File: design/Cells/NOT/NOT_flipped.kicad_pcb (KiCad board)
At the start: 2 copper layers, 2 parts, among them P1 Q_PJFET_GSD

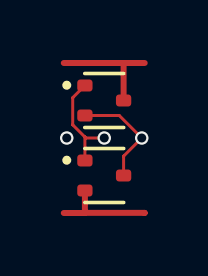
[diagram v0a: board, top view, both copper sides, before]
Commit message: All gates layout on a strict 2.5mm grid. Flipped versions of all three layouts
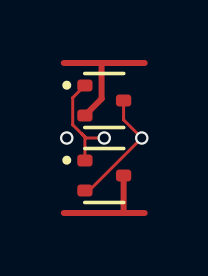
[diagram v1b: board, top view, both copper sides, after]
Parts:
- moved N1 2.50 mm to (1.25, 1.25)
- moved P1 2.50 mm to (1.25, 3.75)
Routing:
- net GND: track 3.45 -> 4.68 mm
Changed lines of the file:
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@@
 	(footprint "Package_TO_SOT_SMD:SOT-523"
 		(layer "F.Cu")
-		(at 1.25 1.25)
+		(at 1.25 3.75)
 		(descr "SOT523, https://www.diodes.com/assets/Package-Files/SOT523.pdf")
 		(tags "SOT-523")
@@
 	(footprint "Package_TO_SOT_SMD:SOT-523"
 		(layer "F.Cu")
-		(at 1.25 3.75)
+		(at 1.25 1.25)
 		(descr "SOT523, https://www.diodes.com/assets/Package-Files/SOT523.pdf")
 		(tags "SOT-523")
@@
 	)
 	(segment
-		(start 1.895 3.105)
-		(end 1.895 3.75)
+		(start 0.75 4.25)
+		(end 0.605 4.25)
 		(width 0.1)
 		(layer "F.Cu")
@@
 	)
 	(segment
-		(start 1.75 1.75)
+		(start 1.895 1.25)
+		(end 1.895 1.895)
+		(width 0.1)
+		(layer "F.Cu")
+		(net 1)
+	)
+	(segment
+		(start 1.895 1.895)
 		(end 2.5 2.5)
 		(width 0.1)
@@
 	)
 	(segment
-		(start 0.605 1.75)
-		(end 1.75 1.75)
-		(width 0.1)
-		(layer "F.Cu")
-		(net 1)
-	)
-	(segment
 		(start 2.5 2.5)
-		(end 1.895 3.105)
+		(end 0.75 4.25)
 		(width 0.1)
 		(layer "F.Cu")
@@
 	)
 	(segment
-		(start 0.605 4.995)
-		(end 2.595 4.995)
+		(start -0.1 0)
+		(end 2.6 0)
 		(width 0.2)
 		(layer "F.Cu")
@@
 	)
 	(segment
-		(start 0.605 4.995)
-		(end 0.6 5)
+		(start 1.161 1.194)
+		(end 1.161 0.011)
 		(width 0.2)
 		(layer "F.Cu")
@@
 	)
 	(segment
-		(start 2.595 4.995)
-		(end 2.6 5)
+		(start 0.605 1.75)
+		(end 1.161 1.194)
 		(width 0.2)
 		(layer "F.Cu")
@@
 	)
 	(segment
-		(start 0.605 4.25)
-		(end 0.605 4.995)
+		(start 1.161 0.011)
+		(end 1.15 0)
 		(width 0.2)
 		(layer "F.Cu")
@@
 	)
 	(segment
-		(start 0.6 5)
-		(end -0.1 5)
-		(width 0.2)
-		(layer "F.Cu")
-		(net 2)
+		(start 0.199 1.156)
+		(end 0.199 2.061189)
+		(width 0.1)
+		(layer "F.Cu")
+		(net 3)
+	)
+	(segment
+		(start 0.605 0.75)
+		(end 0.199 1.156)
+		(width 0.1)
+		(layer "F.Cu")
+		(net 3)
+	)
+	(segment
+		(start 1.25 2.5)
+		(end 0.637812 2.5)
+		(width 0.1)
+		(layer "F.Cu")
+		(net 3)
+	)
+	(segment
+		(start 0.493906 2.356094)
+		(end 0.605 2.467189)
+		(width 0.1)
+		(layer "F.Cu")
+		(net 3)
 	)
 	(segment
@@
 	)
 	(segment
+		(start 0.637812 2.5)
+		(end 0.493906 2.356094)
+		(width 0.1)
+		(layer "F.Cu")
+		(net 3)
+	)
+	(segment
 		(start 0.199 2.061189)
-		(end 0.605 2.467189)
-		(width 0.1)
-		(layer "F.Cu")
-		(net 3)
-	)
-	(segment
-		(start 0.637811 2.5)
-		(end 0.605 2.467189)
-		(width 0.1)
-		(layer "F.Cu")
-		(net 3)
-	)
-	(segment
-		(start 0.199 1.156)
-		(end 0.199 2.061189)
-		(width 0.1)
-		(layer "F.Cu")
-		(net 3)
-	)
-	(segment
-		(start 1.25 2.5)
-		(end 0.637811 2.5)
-		(width 0.1)
-		(layer "F.Cu")
-		(net 3)
-	)
-	(segment
-		(start 0.605 0.75)
-		(end 0.199 1.156)
+		(end 0.493906 2.356094)
 		(width 0.1)
 		(layer "F.Cu")
@@
 	)
 	(segment
-		(start 1.9 0)
-		(end 2.6 0)
+		(start -0.1 5)
+		(end 2.6 5)
 		(width 0.2)
 		(layer "F.Cu")
@@
 	)
 	(segment
-		(start 1.9 0)
-		(end -0.1 0)
+		(start 1.895 3.75)
+		(end 1.895 4.995)
 		(width 0.2)
 		(layer "F.Cu")
@@
 	)
 	(segment
-		(start 1.895 1.25)
-		(end 1.895 0.005)
-		(width 0.2)
-		(layer "F.Cu")
+		(start 1.895 4.995)
+		(end 1.9 5)
+		(width 0.2)
+		(layer "F.Cu")
